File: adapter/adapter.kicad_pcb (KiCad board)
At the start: 2 copper layers, 96 x 18 mm, 24 parts, among them J1 MALE, J11 MALE, J12 FEMALE, J13 STANDOFF, J14 STANDOFF, J15 STANDOFF, J2 FEMALE, J3 STANDOFF, J4 STANDOFF, J5 STANDOFF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

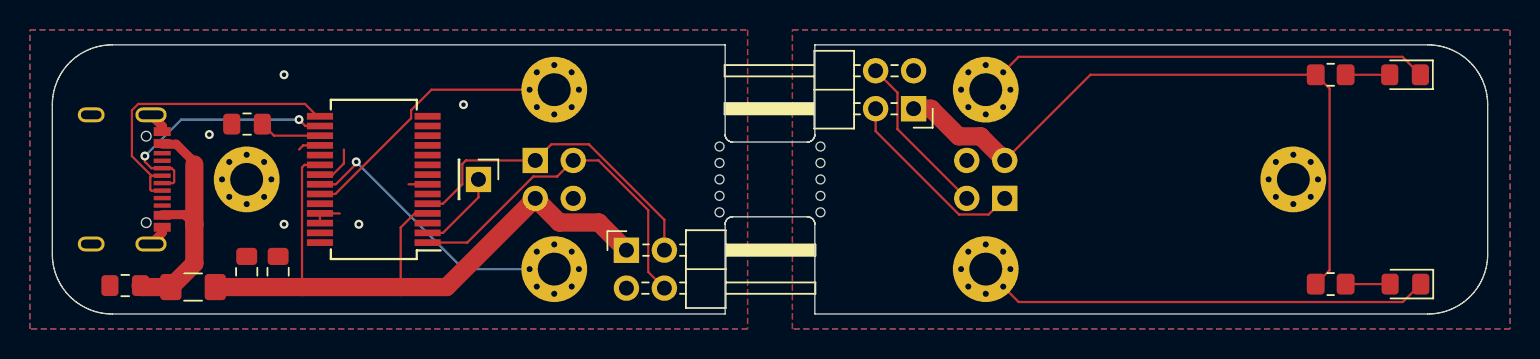
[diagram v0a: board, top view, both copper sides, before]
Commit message: Add new footprints, connect upper standoff
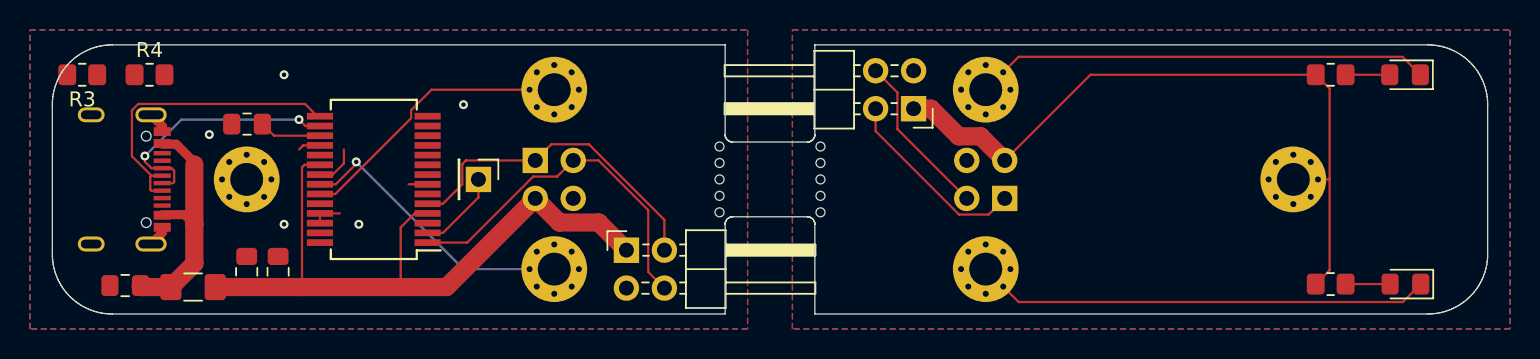
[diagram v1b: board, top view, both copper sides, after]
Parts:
- added R3: 56k, Resistor_SMD:R_0805_2012Metric_Pad1.20x1.40mm_HandSolder, F.Cu at (102.5, 98.0)
- added R4: 56k, Resistor_SMD:R_0805_2012Metric_Pad1.20x1.40mm_HandSolder, F.Cu at (107.0, 98.0)
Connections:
- J15 pad 1: Net-(J15-Pad1) -> +5V
- J5 pad 1: Net-(J5-Pad1) -> +5VB
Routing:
- net +5V: track 45.5 -> 47.9 mm

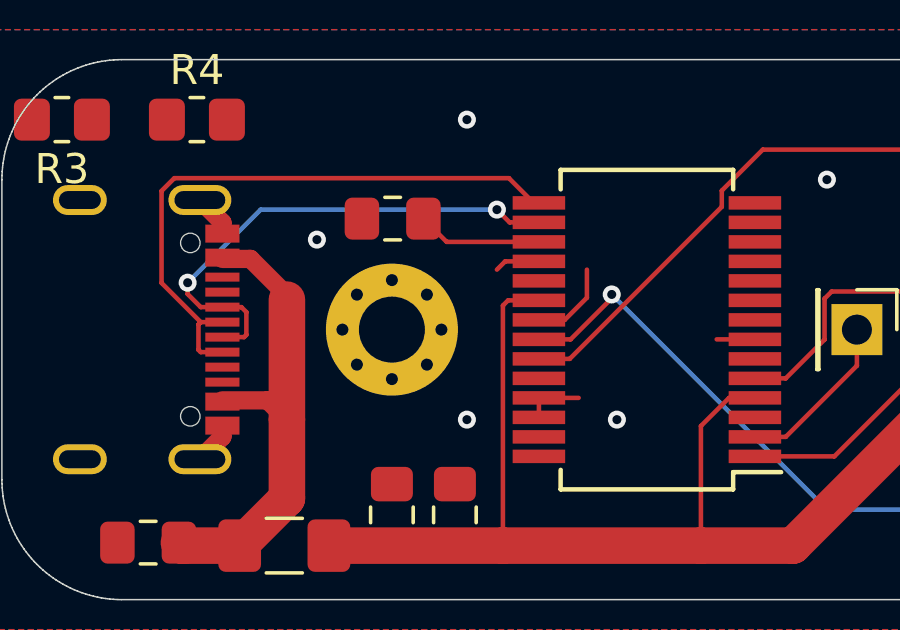
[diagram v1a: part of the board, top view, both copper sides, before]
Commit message: Connect lower standoff
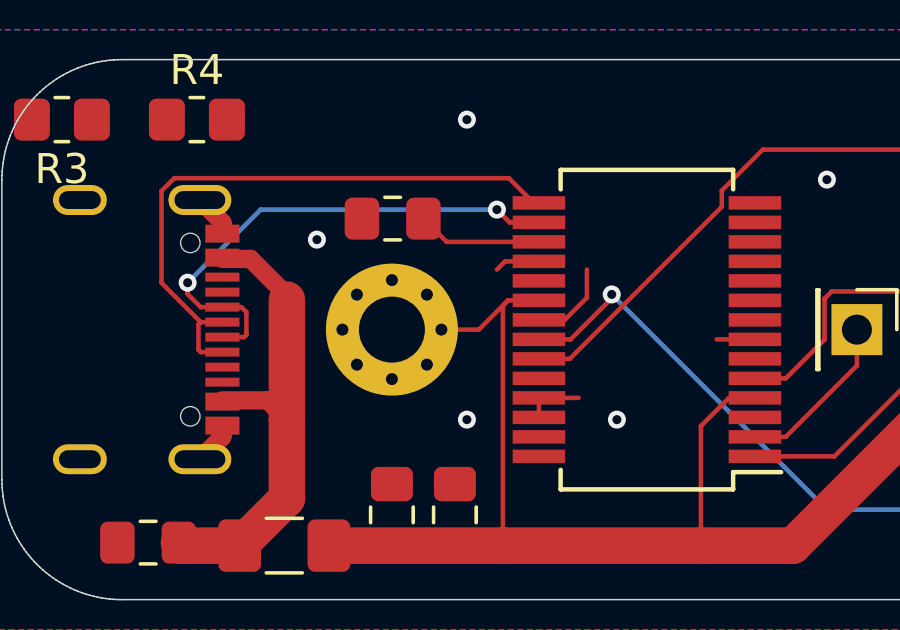
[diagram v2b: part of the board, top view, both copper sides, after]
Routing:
- net +5VB: track 46.8 -> 51.1 mm
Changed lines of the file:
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@@
     (thickness 1.6)
     (drawings 392)
-    (tracks 126)
+    (tracks 128)
     (zones 0)
     (modules 26)
@@
   (segment (start 124.738518 107.275) (end 123.8 108.213518) (width 0.1524) (layer F.Cu) (net 34))
   (segment (start 126.87 112.2) (end 123.8 112.2) (width 1.2192) (layer F.Cu) (net 34))
+  (segment (start 116.3976 105) (end 117.3726 104.025) (width 0.1524) (layer F.Cu) (net 34))
+  (segment (start 113.5 105) (end 116.3976 105) (width 0.1524) (layer F.Cu) (net 34))
   (zone (net 2) (net_name GND) (layer B.Cu) (hatch edge 0.508)
     (connect_pads (clearance 0.508))
